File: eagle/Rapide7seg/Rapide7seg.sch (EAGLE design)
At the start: 47 parts, among them IC1 MEGA8-P, J1 AVR_SPI_PRG_6PTH

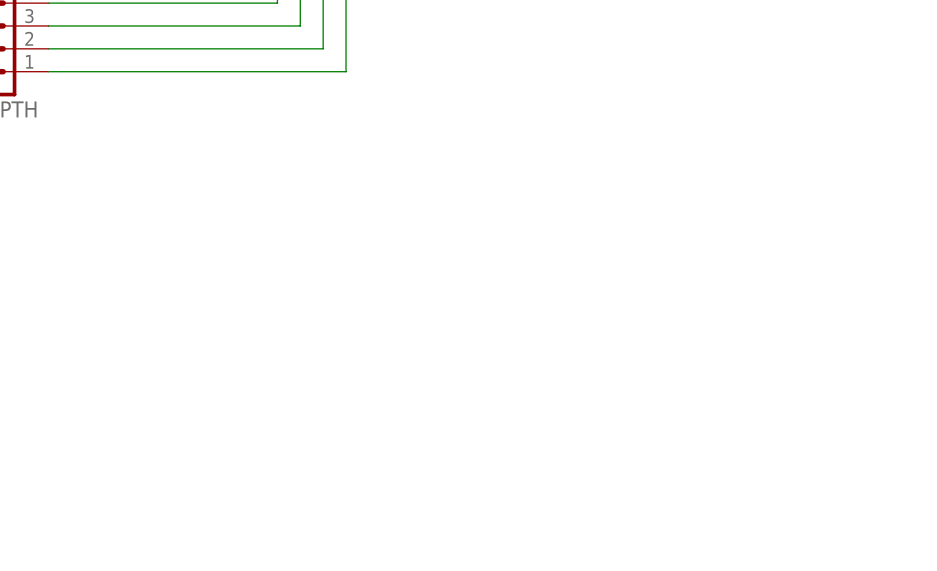
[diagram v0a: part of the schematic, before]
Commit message: edit/bugfix (wrongly used vias instead of pins)
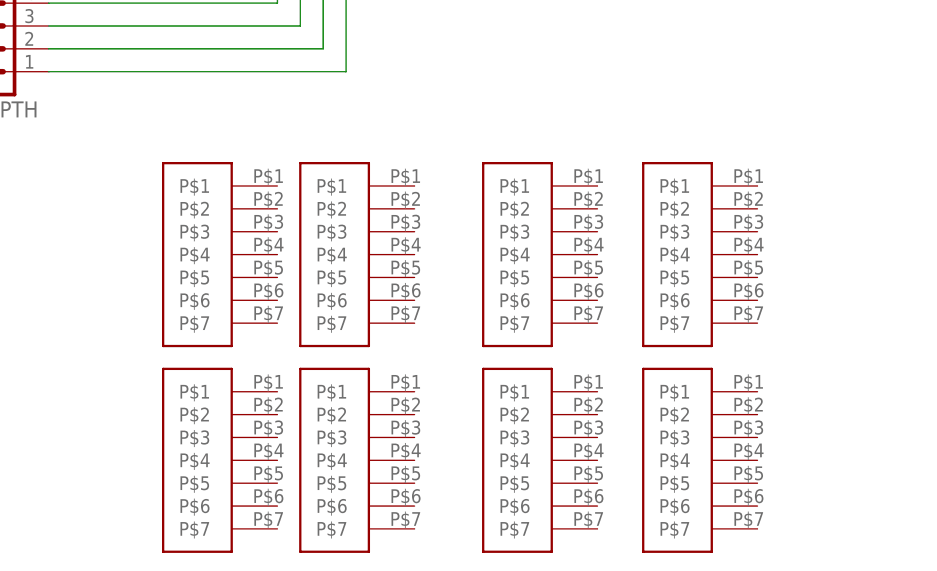
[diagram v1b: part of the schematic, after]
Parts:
- added U$1, U$2, U$3, U$4, U$5, U$6, U$7, U$8: M7_NOSILK, kalshagar:M7_NOSILK
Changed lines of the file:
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@@
 <layer number="144" name="Drill_legend" color="7" fill="1" visible="no" active="yes"/>
 <layer number="151" name="HeatSink" color="7" fill="1" visible="no" active="yes"/>
+<layer number="199" name="Contour" color="7" fill="1" visible="yes" active="yes"/>
 <layer number="200" name="200bmp" color="1" fill="10" visible="no" active="yes"/>
 <layer number="201" name="201bmp" color="2" fill="10" visible="no" active="yes"/>
@@
 <part name="JPVCC" library="SparkFun" deviceset="M02" device="PTH"/>
 <part name="C3" library="resistor" deviceset="CPOL-EU" device="E1.8-4"/>
+<part name="U$1" library="kalshagar" deviceset="M7_NOSILK" device=""/>
+<part name="U$2" library="kalshagar" deviceset="M7_NOSILK" device=""/>
+<part name="U$3" library="kalshagar" deviceset="M7_NOSILK" device=""/>
+<part name="U$4" library="kalshagar" deviceset="M7_NOSILK" device=""/>
+<part name="U$5" library="kalshagar" deviceset="M7_NOSILK" device=""/>
+<part name="U$6" library="kalshagar" deviceset="M7_NOSILK" device=""/>
+<part name="U$7" library="kalshagar" deviceset="M7_NOSILK" device=""/>
+<part name="U$8" library="kalshagar" deviceset="M7_NOSILK" device=""/>
 </parts>
 <sheets>
@@
 <instance part="JPVCC" gate="G$1" x="-195.58" y="0"/>
 <instance part="C3" gate="G$1" x="-162.56" y="27.94"/>
+<instance part="U$1" gate="G$1" x="-121.92" y="-17.78"/>
+<instance part="U$2" gate="G$1" x="-121.92" y="-40.64"/>
+<instance part="U$3" gate="G$1" x="-106.68" y="-17.78"/>
+<instance part="U$4" gate="G$1" x="-106.68" y="-40.64"/>
+<instance part="U$5" gate="G$1" x="-86.36" y="-17.78"/>
+<instance part="U$6" gate="G$1" x="-86.36" y="-40.64"/>
+<instance part="U$7" gate="G$1" x="-68.58" y="-17.78"/>
+<instance part="U$8" gate="G$1" x="-68.58" y="-40.64"/>
 </instances>
 <busses>
